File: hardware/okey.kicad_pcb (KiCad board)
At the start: 2 copper layers, 243.8 x 352.4 mm, 115 parts, among them IC1 4094N, IC2 4094N, P1 ROW_JMP, P10 CONN_02X06, P11 CONN_02X06, P12 CONN_02X06, P13 CONN_02X06, P14 CONN_02X06, P15 CONN_02X06, P16 CONN_02X08, P17 CONN_01X01, P18 CONN_02X08, P19 CONN_01X01, P2 CONN_02X13, P20 CONN_01X01, P21 CONN_01X01, P22 CONN_02X08, P23 CONN_02X08, P24 CONN_02X06, P25 CONN_02X06, P26 CONN_02X06, P27 CONN_02X06, P28 CONN_02X06, P29 CONN_02X06, P3 CONN_02X03, P30 CONN_02X08, P31 CONN_02X03, P4 CONN_02X08, P5 CONN_02X03, P6 CONN_02X10, P7 CONN_02X03, P8 CONN_01X01, P9 CONN_02X08, Q1 Q_NPN_BCE, Q2 Q_NPN_BCE, Q3 Q_NPN_BCE, SW1 MX_D, SW10 MX_D, SW11 MX_D, SW12 MX_D, SW13 MX_D, SW14 MX_D, SW15 MX_D, SW16 MX_D, SW17 MX_D, SW18 MX_D, SW19 SW_PUSH, SW2 MX_D, SW20 SW_PUSH, SW21 SW_PUSH, SW22 SW_PUSH, SW23 SW_PUSH, SW24 SW_PUSH, SW25 SW_PUSH, SW26 SW_PUSH, SW27 SW_PUSH, SW28 SW_PUSH, SW29 SW_PUSH, SW3 MX_D, SW30 SW_PUSH, SW31 SW_PUSH, SW32 SW_PUSH, SW33 SW_PUSH, SW34 SW_PUSH, SW35 MX_D, SW36 MX_D, SW37 MX_D, SW38 MX_D, SW39 MX_D, SW4 MX_D, SW5 MX_D, SW6 MX_D, SW7 MX_D, SW8 MX_D, SW9 MX_D, U1 4053, U2 4024, U3 TEENSY2.0

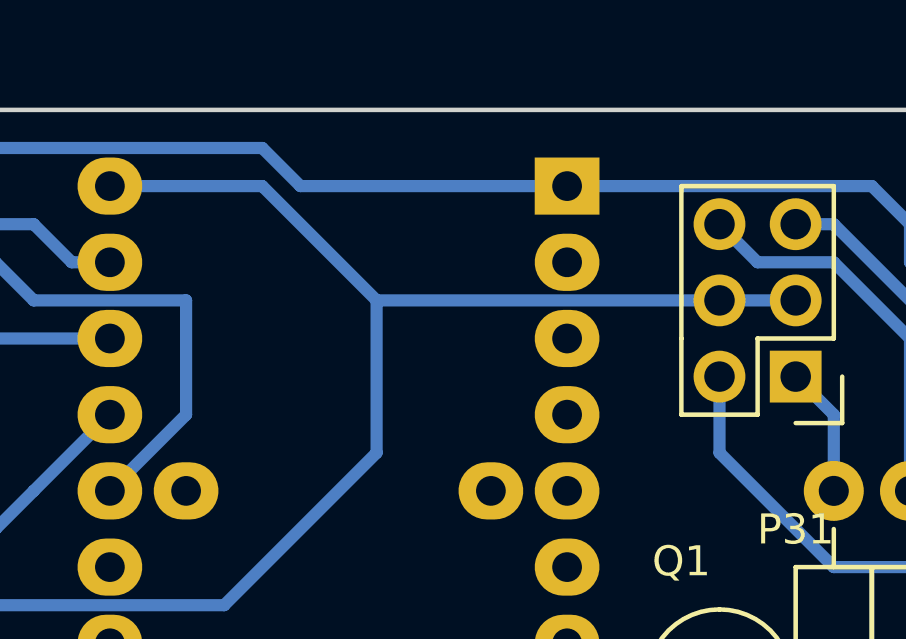
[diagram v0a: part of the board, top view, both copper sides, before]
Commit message: PCB fix: add pullup resistor
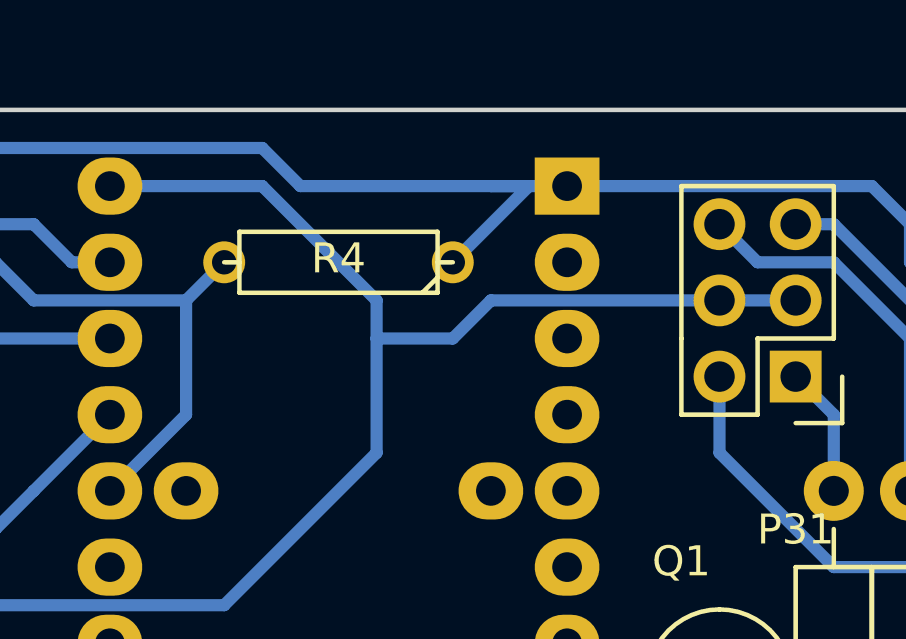
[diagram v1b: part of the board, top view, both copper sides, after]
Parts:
- added R4: R, Discret:R3, F.Cu at (142.2, 21.6)
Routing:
- net Net-(P7-Pad2): track 83.8 -> 88.6 mm
- net Net-(P7-Pad4): track 15.5 -> 17.3 mm
- net Net-(D25-Pad2): track 58.1 -> 58.6 mm
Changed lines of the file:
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@@
 (kicad_pcb (version 4) (host pcbnew 4.0.1-stable)
   (general
-    (links 547)
+    (links 549)
     (no_connects 98)
-    (area 15.164999 12.9234 259.075001 367.762501)
+    (area 15.164999 15.164999 259.075001 367.762501)
     (thickness 1.6)
     (drawings 49)
-    (tracks 1633)
+    (tracks 1640)
     (zones 0)
-    (modules 115)
+    (modules 116)
     (nets 210)
   )
@@
     )
   )
+  (module Discret:R3 (layer F.Cu)
+    (at 142.24 21.59 180)
+    (descr "Resitance 3 pas")
+    (tags R)
+    (fp_text reference R4 (at 0 0.127 180) (layer F.SilkS)
+      (effects (font (size 1 1) (thickness 0.15)))
+    )
+    (fp_text value R (at 0 0.127 180) (layer F.Fab)
+      (effects (font (size 1 1) (thickness 0.15)))
+    )
+    (fp_line (start -3.81 0) (end -3.302 0) (layer F.SilkS) (width 0.15))
+    (fp_line (start 3.81 0) (end 3.302 0) (layer F.SilkS) (width 0.15))
+    (fp_line (start 3.302 0) (end 3.302 -1.016) (layer F.SilkS) (width 0.15))
+    (fp_line (start 3.302 -1.016) (end -3.302 -1.016) (layer F.SilkS) (width 0.15))
+    (fp_line (start -3.302 -1.016) (end -3.302 1.016) (layer F.SilkS) (width 0.15))
+    (fp_line (start -3.302 1.016) (end 3.302 1.016) (layer F.SilkS) (width 0.15))
+    (fp_line (start 3.302 1.016) (end 3.302 0) (layer F.SilkS) (width 0.15))
+    (fp_line (start -3.302 -0.508) (end -2.794 -1.016) (layer F.SilkS) (width 0.15))
+    (pad 1 thru_hole circle (at -3.81 0 180) (size 1.397 1.397) (drill 0.8128) (layers *.Cu *.Mask F.SilkS)
+      (net 116 "Net-(P7-Pad2)"))
+    (pad 2 thru_hole circle (at 3.81 0 180) (size 1.397 1.397) (drill 0.8128) (layers *.Cu *.Mask F.SilkS)
+      (net 118 "Net-(P7-Pad4)"))
+    (model Discret.3dshapes/R3.wrl
+      (at (xyz 0 0 0))
+      (scale (xyz 0.3 0.3 0.3))
+      (rotate (xyz 0 0 0))
+    )
+  )
   (gr_circle (center 255.53125 335.3125) (end 255.53125 334.15625) (layer Edge.Cuts) (width 0.15))
   (gr_circle (center 21.96875 335.3125) (end 21.96875 334.15625) (layer Edge.Cuts) (width 0.15))
@@
   (segment (start 132.08 20.32) (end 133.35 21.59) (width 0.4064) (layer B.Cu) (net 115))
   (segment (start 128.27 20.32) (end 132.08 20.32) (width 0.4064) (layer B.Cu) (net 115))
+  (segment (start 146.05 21.59) (end 148.59 19.05) (width 0.4064) (layer B.Cu) (net 116) (status 400000))
+  (segment (start 148.59 19.05) (end 147.32 19.05) (width 0.4064) (layer B.Cu) (net 116))
   (segment (start 161.29 20.32) (end 161.29 21.59) (width 0.4064) (layer B.Cu) (net 116))
   (segment (start 162.56 22.86) (end 163.83 22.86) (width 0.4064) (layer B.Cu) (net 116))
@@
   (segment (start 160.02 19.05) (end 161.29 20.32) (width 0.4064) (layer B.Cu) (net 116))
   (segment (start 163.83 22.86) (end 166.37 25.4) (width 0.4064) (layer B.Cu) (net 116))
-  (segment (start 149.86 19.05) (end 140.97 19.05) (width 0.4064) (layer B.Cu) (net 116))
+  (segment (start 149.86 19.05) (end 147.32 19.05) (width 0.4064) (layer B.Cu) (net 116))
+  (segment (start 147.32 19.05) (end 140.97 19.05) (width 0.4064) (layer B.Cu) (net 116))
   (segment (start 130.81 17.78) (end 129.54 19.05) (width 0.4064) (layer B.Cu) (net 116))
   (segment (start 139.7 17.78) (end 130.81 17.78) (width 0.4064) (layer B.Cu) (net 116))
@@
   (segment (start 128.27 25.4) (end 128.27 22.86) (width 0.4064) (layer B.Cu) (net 117))
   (segment (start 134.62 26.67) (end 132.08 29.21) (width 0.4064) (layer B.Cu) (net 117))
+  (segment (start 137.16 22.86) (end 138.43 21.59) (width 0.4064) (layer B.Cu) (net 118) (status 800000))
   (segment (start 134.62 29.21) (end 137.16 26.67) (width 0.4064) (layer B.Cu) (net 118))
   (segment (start 130.81 21.59) (end 129.54 21.59) (width 0.4064) (layer B.Cu) (net 118))
@@
   (segment (start 158.75 20.32) (end 157.48 20.32) (width 0.4064) (layer B.Cu) (net 206))
   (segment (start 163.83 25.4) (end 158.75 20.32) (width 0.4064) (layer B.Cu) (net 206))
-  (segment (start 143.51 22.86) (end 154.94 22.86) (width 0.4064) (layer B.Cu) (net 207))
+  (segment (start 147.32 22.86) (end 146.05 24.13) (width 0.4064) (layer B.Cu) (net 207))
+  (segment (start 146.05 24.13) (end 143.51 24.13) (width 0.4064) (layer B.Cu) (net 207))
+  (segment (start 147.32 22.86) (end 154.94 22.86) (width 0.4064) (layer B.Cu) (net 207))
   (segment (start 154.94 22.86) (end 157.48 22.86) (width 0.4064) (layer B.Cu) (net 207))
-  (segment (start 143.51 22.86) (end 143.51 27.94) (width 0.4064) (layer B.Cu) (net 207))
+  (segment (start 143.51 22.86) (end 143.51 24.13) (width 0.4064) (layer B.Cu) (net 207))
+  (segment (start 143.51 24.13) (end 143.51 27.94) (width 0.4064) (layer B.Cu) (net 207))
+  (segment (start 138.43 33.02) (end 127 33.02) (width 0.4064) (layer B.Cu) (net 207))
+  (segment (start 125.73 25.4) (end 125.73 31.75) (width 0.4064) (layer B.Cu) (net 207))
+  (segment (start 125.73 31.75) (end 127 33.02) (width 0.4064) (layer B.Cu) (net 207))
+  (segment (start 127 24.13) (end 125.73 25.4) (width 0.4064) (layer B.Cu) (net 207))
   (segment (start 143.51 27.94) (end 138.43 33.02) (width 0.4064) (layer B.Cu) (net 207))
   (segment (start 143.51 22.86) (end 139.7 19.05) (width 0.4064) (layer B.Cu) (net 207))
-  (segment (start 127 24.13) (end 125.73 25.4) (width 0.4064) (layer B.Cu) (net 207))
-  (segment (start 125.73 31.75) (end 127 33.02) (width 0.4064) (layer B.Cu) (net 207))
-  (segment (start 125.73 25.4) (end 125.73 31.75) (width 0.4064) (layer B.Cu) (net 207))
-  (segment (start 138.43 33.02) (end 127 33.02) (width 0.4064) (layer B.Cu) (net 207))
   (segment (start 139.7 19.05) (end 134.62 19.05) (width 0.4064) (layer B.Cu) (net 207))
   (segment (start 158.75 29.21) (end 158.75 26.67) (width 0.4064) (layer B.Cu) (net 208))
@@
     (connect_pads (clearance 0.508))
     (min_thickness 0.254)
-    (fill yes (arc_segments 16) (thermal_gap 0.508) (thermal_bridge_width 0.508))
+    (fill (arc_segments 16) (thermal_gap 0.508) (thermal_bridge_width 0.508))
     (polygon
       (pts
@@
     (connect_pads (clearance 0.508))
     (min_thickness 0.254)
-    (fill yes (arc_segments 16) (thermal_gap 0.508) (thermal_bridge_width 0.508))
+    (fill (arc_segments 16) (thermal_gap 0.508) (thermal_bridge_width 0.508))
     (polygon
       (pts
@@
     (connect_pads (clearance 0.508))
     (min_thickness 0.254)
-    (fill yes (arc_segments 16) (thermal_gap 0.508) (thermal_bridge_width 0.508))
+    (fill (arc_segments 16) (thermal_gap 0.508) (thermal_bridge_width 0.508))
     (polygon
       (pts
@@
     (connect_pads (clearance 0.508))
     (min_thickness 0.254)
-    (fill yes (arc_segments 16) (thermal_gap 0.508) (thermal_bridge_width 0.508))
+    (fill (arc_segments 16) (thermal_gap 0.508) (thermal_bridge_width 0.508))
     (polygon
       (pts
@@
     (connect_pads (clearance 0.508))
     (min_thickness 0.254)
-    (fill yes (arc_segments 16) (thermal_gap 0.508) (thermal_bridge_width 0.508))
+    (fill (arc_segments 16) (thermal_gap 0.508) (thermal_bridge_width 0.508))
     (polygon
       (pts
@@
     (connect_pads (clearance 0.508))
     (min_thickness 0.254)
-    (fill yes (arc_segments 16) (thermal_gap 0.508) (thermal_bridge_width 0.508))
+    (fill (arc_segments 16) (thermal_gap 0.508) (thermal_bridge_width 0.508))
     (polygon
       (pts

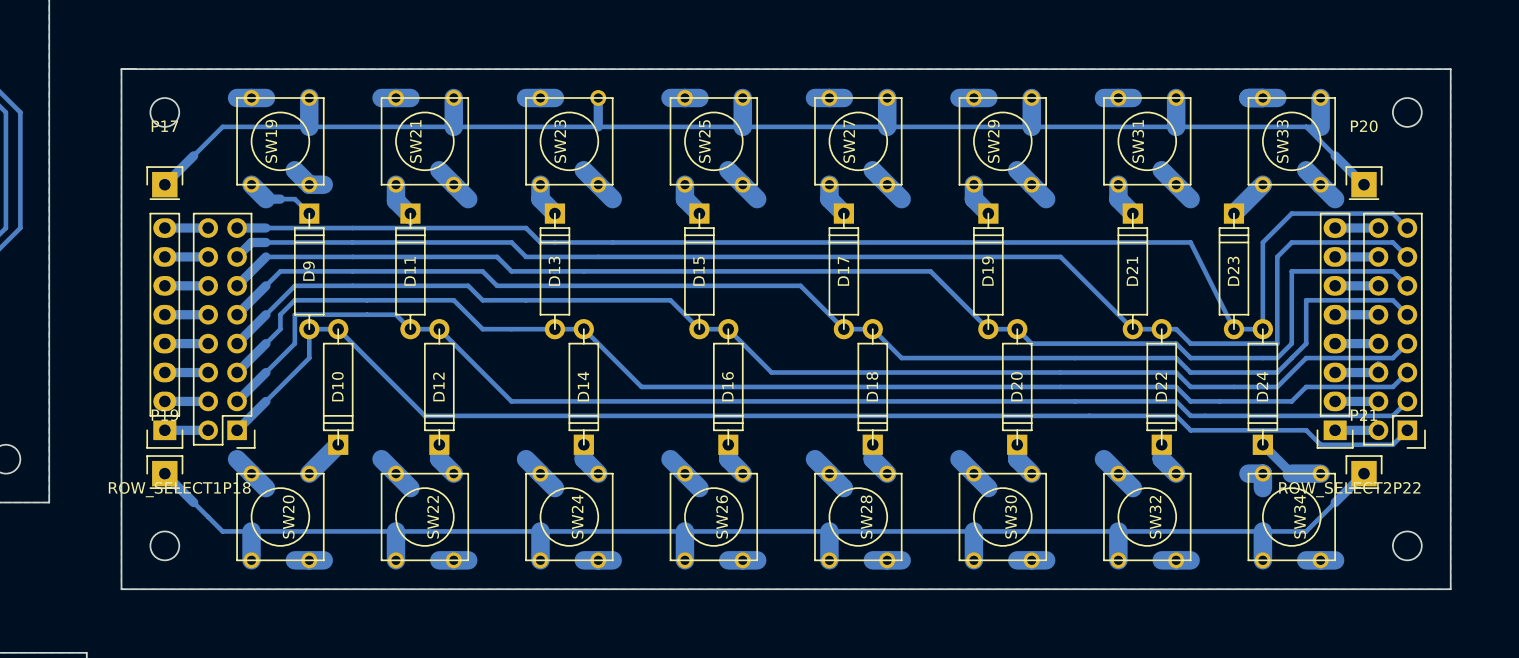
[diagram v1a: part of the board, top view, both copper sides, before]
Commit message: PCB fix: dimensions on extra button board
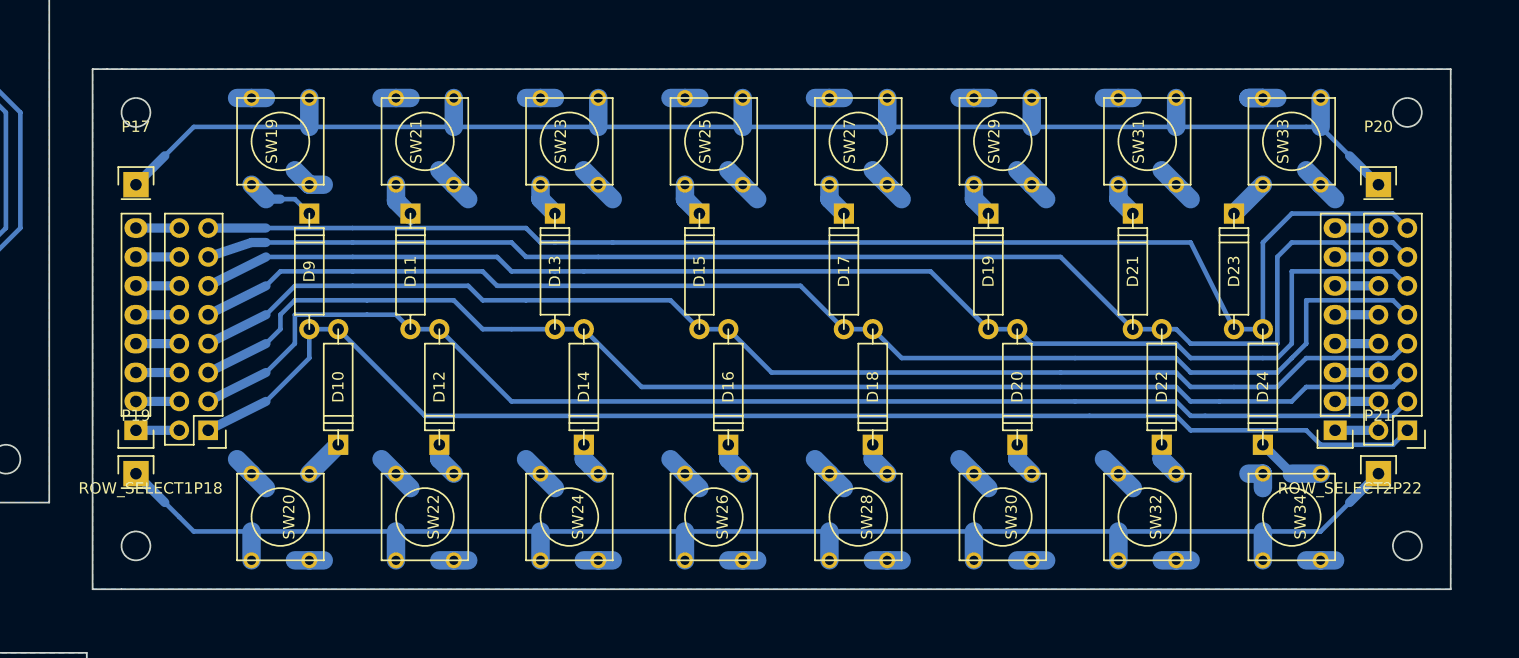
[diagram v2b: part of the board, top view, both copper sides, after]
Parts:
- moved P17 2.54 mm to (125.7, 69.8)
- moved P19 2.54 mm to (125.7, 95.2)
- moved ROW_SELECT1 2.54 mm to (125.7, 91.4)
- moved P18 2.54 mm to (132.1, 91.4)
- moved P20 1.27 mm to (234.9, 69.8)
- moved P21 1.27 mm to (234.9, 95.2)
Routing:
- net Net-(P19-Pad1): track 157.6 -> 161.4 mm
- net Net-(P17-Pad1): track 159.4 -> 162.0 mm
- net Net-(D23-Pad2): track 117.3 -> 119.8 mm
- net Net-(D21-Pad2): track 115.8 -> 118.0 mm
- net Net-(D17-Pad2): track 113.5 -> 115.6 mm
- net Net-(D15-Pad2): track 110.2 -> 112.3 mm
- net Net-(D11-Pad2): track 111.7 -> 113.8 mm
- net Net-(D19-Pad2): track 115.0 -> 117.1 mm
- net Net-(D13-Pad2): track 111.0 -> 113.1 mm
- net Net-(D10-Pad2): track 112.8 -> 114.9 mm
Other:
- outline, holes or cut-outs redrawn

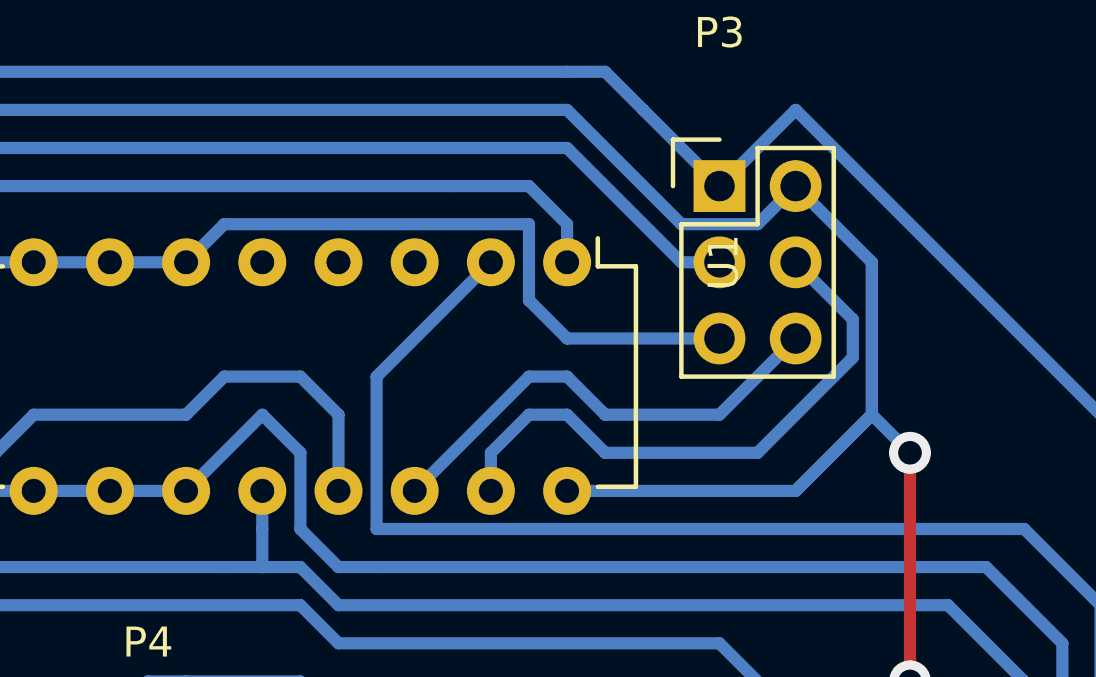
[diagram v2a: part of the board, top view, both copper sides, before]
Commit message: PCD design: increase distance of too close wires
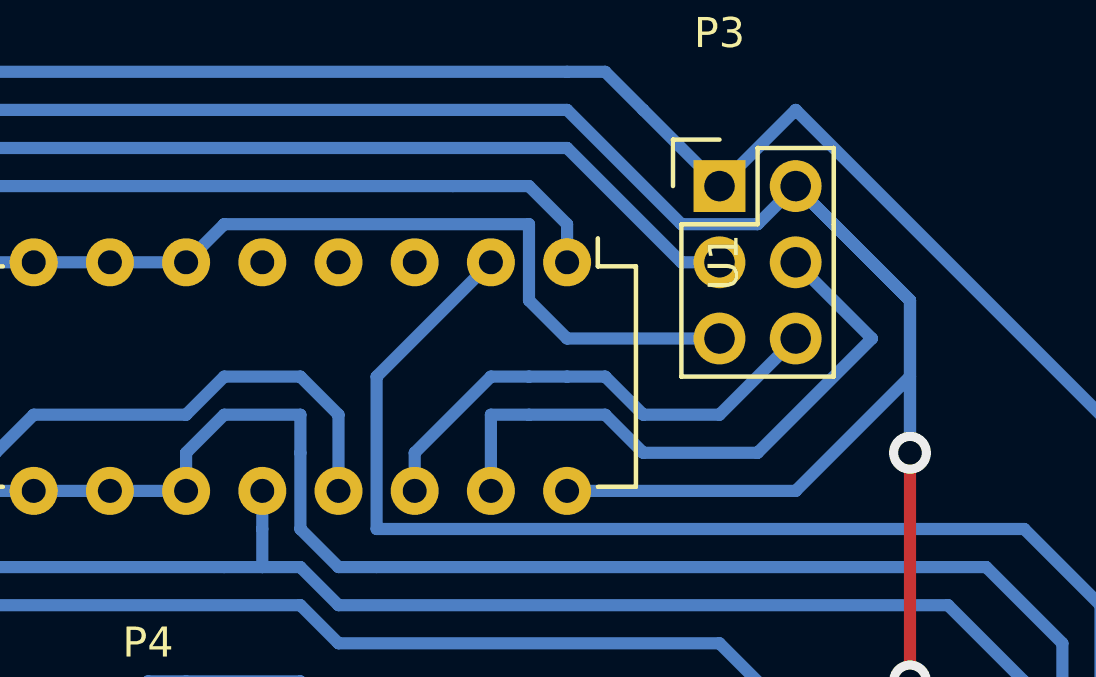
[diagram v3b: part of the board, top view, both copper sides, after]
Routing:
- net VDD: track 418.4 -> 423.8 mm
- net Net-(IC1-Pad1): track 248.7 -> 250.2 mm
- net Net-(P3-Pad4): track 19.7 -> 20.9 mm
- net Net-(P3-Pad6): track 15.9 -> 16.6 mm
